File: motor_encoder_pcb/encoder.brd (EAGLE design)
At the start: 48.2 x 26.3 mm, 6 parts

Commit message: encoder pcb changes
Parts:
- moved H1 16.5 mm to (-7.62, 47.0)
- moved H2 16.5 mm to (30.5, 47.0)
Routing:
- net GND: track 0.00 -> 17.3 mm
- added copper zone on layer 1, net PLATE
- removed copper zone on layer 1, net GND
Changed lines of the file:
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@@
 </element>
 <element name="U$1" library="ee192" package="S6986" value="S6986" x="12.7" y="46.99" rot="R180"/>
-<element name="H1" library="holes" library_urn="urn:adsk.eagle:library:237" package="3,3" package3d_urn="urn:adsk.eagle:package:14278/1" value="MOUNT-HOLE3.3" x="-7.62" y="63.5"/>
-<element name="H2" library="holes" library_urn="urn:adsk.eagle:library:237" package="3,3" package3d_urn="urn:adsk.eagle:package:14278/1" value="MOUNT-HOLE3.3" x="30.48" y="63.5"/>
+<element name="H1" library="holes" library_urn="urn:adsk.eagle:library:237" package="3,3" package3d_urn="urn:adsk.eagle:package:14278/1" value="MOUNT-HOLE3.3" x="-7.62" y="46.99"/>
+<element name="H2" library="holes" library_urn="urn:adsk.eagle:library:237" package="3,3" package3d_urn="urn:adsk.eagle:package:14278/1" value="MOUNT-HOLE3.3" x="30.48" y="46.99"/>
 </elements>
 <signals>
@@
 <contactref element="U$1" pad="3"/>
 <contactref element="U$1" pad="2"/>
-<polygon width="0.0508" layer="1" isolate="0.762">
-<vertex x="-12.7" y="68.58"/>
-<vertex x="35.56" y="68.58"/>
-<vertex x="35.56" y="41.91"/>
-<vertex x="-12.7" y="41.91"/>
-</polygon>
+<wire x1="13.3" y1="46.99" x2="13.3" y2="57.75" width="0.508" layer="1"/>
+<wire x1="15.24" y1="59.69" x2="15.24" y2="63.5" width="0.508" layer="1"/>
+<wire x1="13.3" y1="57.75" x2="15.24" y2="59.69" width="0.508" layer="1"/>
+<wire x1="12.03" y1="46.99" x2="13.3" y2="46.99" width="0" layer="19" extent="1-1"/>
 </signal>
 <signal name="N$1">
@@
 <wire x1="16.51" y1="46.99" x2="16.51" y2="50.8" width="0.508" layer="1"/>
 </signal>
+<signal name="PLATE">
+<polygon width="0.0508" layer="1" isolate="0.762">
+<vertex x="-12.7" y="68.58"/>
+<vertex x="35.56" y="68.58"/>
+<vertex x="35.56" y="41.91"/>
+<vertex x="-12.7" y="41.91"/>
+</polygon>
+</signal>
 </signals>

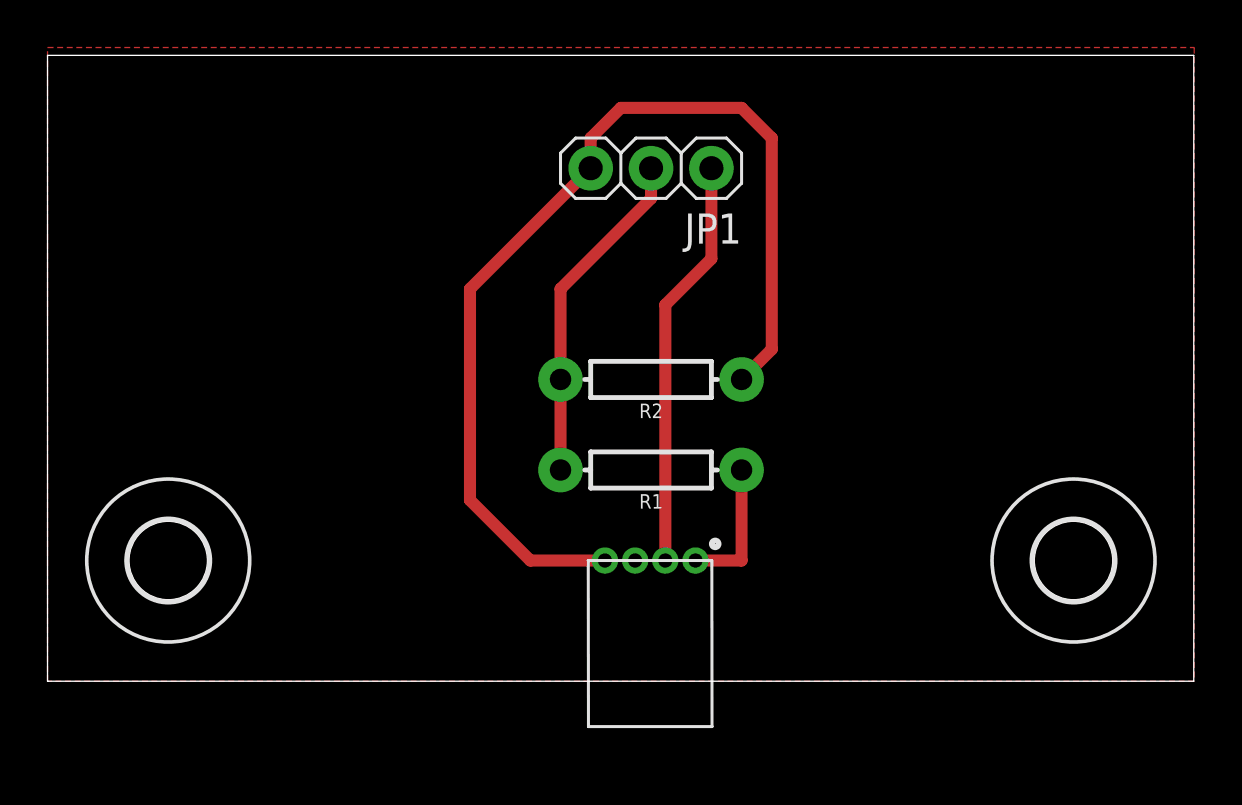
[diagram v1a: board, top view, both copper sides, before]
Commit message: new encoder PCB output
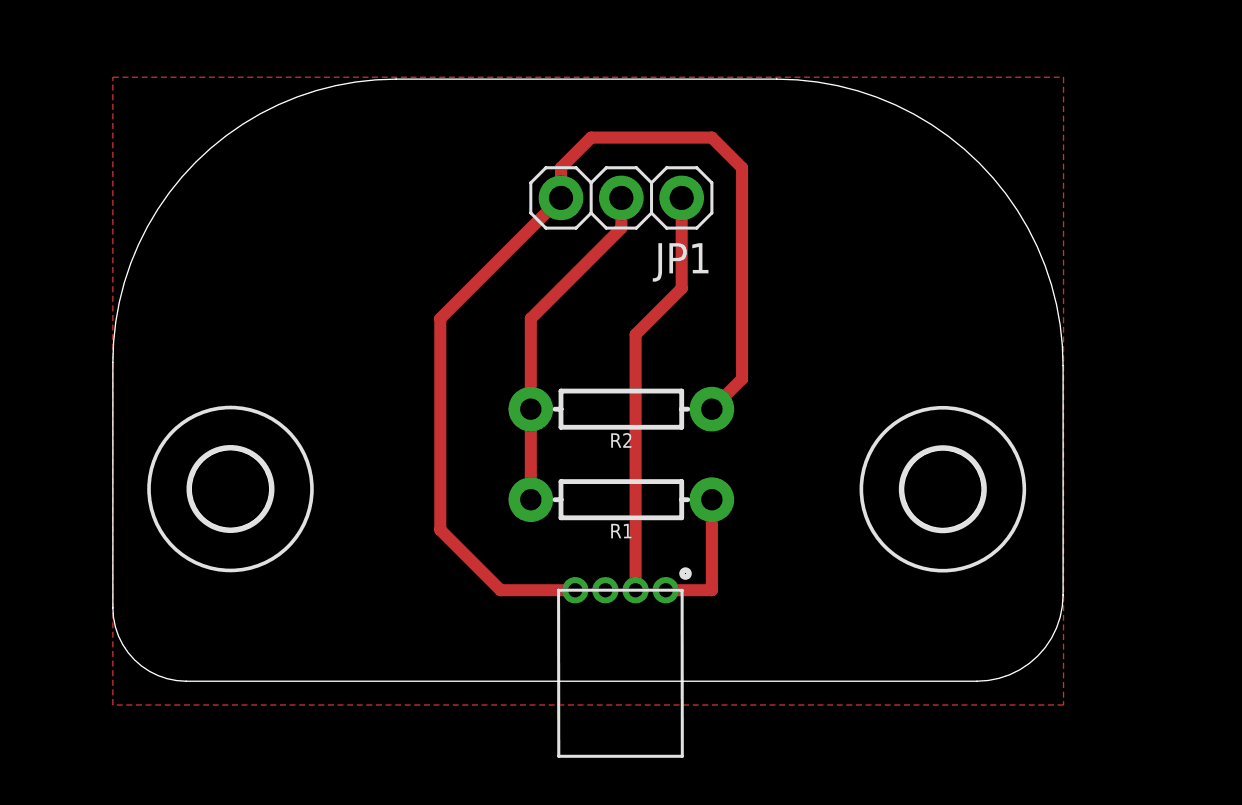
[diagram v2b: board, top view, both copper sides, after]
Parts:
- moved H2 6.26 mm to (25.0, 50.0)
- moved H1 3.99 mm to (-5.00, 50.0)
- moved JP1 1.77 mm to (11.4, 62.2)
- moved R1 1.77 mm to (11.4, 49.5)
- moved R2 1.77 mm to (11.4, 53.4)
- moved U$1 1.77 mm to (11.4, 45.7)
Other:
- board size 48.2 x 26.3 mm -> 40 x 25.3 mm
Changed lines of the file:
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@@
 <setting verticaltext="up"/>
 </settings>
-<grid distance="50" unitdist="mil" unit="mil" style="lines" multiple="2" display="yes" altdistance="5" altunitdist="mil" altunit="mil"/>
+<grid distance="5" unitdist="mm" unit="mm" style="lines" multiple="1" display="yes" altdistance="0.25" altunitdist="mm" altunit="mm"/>
 <layers>
 <layer number="1" name="Top" color="4" fill="1" visible="yes" active="yes"/>
@@
 <board>
 <plain>
-<wire x1="-12.7" y1="41.91" x2="35.54" y2="41.91" width="0" layer="20"/>
-<wire x1="35.54" y1="41.91" x2="35.54" y2="68.25" width="0" layer="20"/>
-<wire x1="35.54" y1="68.25" x2="-12.7" y2="68.25" width="0" layer="20"/>
-<wire x1="-12.7" y1="68.25" x2="-12.7" y2="41.91" width="0" layer="20"/>
+<wire x1="-9.95" y1="55.330353125" x2="-9.95" y2="45" width="0" layer="20"/>
+<wire x1="-9.95" y1="45" x2="-6.86" y2="41.91" width="0" layer="20" curve="90"/>
+<wire x1="-6.86" y1="41.91" x2="26.41303125" y2="41.91" width="0" layer="20"/>
+<wire x1="26.41303125" y1="41.91" x2="30.04" y2="45.53696875" width="0" layer="20" curve="90"/>
+<wire x1="30.04" y1="45.53696875" x2="30.04" y2="55.197646875" width="0" layer="20"/>
+<wire x1="30.04" y1="55.197646875" x2="17.987646875" y2="67.25" width="0" layer="20" curve="90"/>
+<wire x1="17.987646875" y1="67.25" x2="1.969646875" y2="67.25" width="0" layer="20"/>
+<wire x1="1.969646875" y1="67.25" x2="-9.95" y2="55.330353125" width="0" layer="20" curve="90"/>
 </plain>
 <attributes>
@@
 </class>
 </classes>
-<designrules name="default">
+<designrules name="default *">
 <description language="de">&lt;b&gt;EAGLE Design Rules&lt;/b&gt;
 &lt;p&gt;
@@
 <param name="mdViaViaSameLayer" value="6mil"/>
 <param name="mnLayersViaInSmd" value="2"/>
-<param name="mdCopperDimension" value="40mil"/>
-<param name="mdDrill" value="6mil"/>
+<param name="mdCopperDimension" value="0mil"/>
+<param name="mdDrill" value="2mil"/>
 <param name="mdSmdStop" value="0mil"/>
 <param name="msWidth" value="6mil"/>
@@
 </autorouter>
 <elements>
-<element name="JP1" library="ee192" package="1X03" value="" x="12.7" y="63.5" rot="R180">
-<attribute name="PIE-INT-REF-NUM" value="BULK-STOCK" x="12.7" y="63.5" size="1.778" layer="27" rot="R180" display="off"/>
+<element name="JP1" library="ee192" package="1X03" value="" x="11.45" y="62.25" rot="R180">
+<attribute name="PIE-INT-REF-NUM" value="BULK-STOCK" x="11.45" y="62.25" size="1.778" layer="27" rot="R180" display="off"/>
 </element>
-<element name="R1" library="SparkFun-Resistors" package="AXIAL-0.3" value="150" x="12.7" y="50.8" rot="R180">
-<attribute name="PROD_ID" value="RES-12180" x="12.7" y="50.8" size="1.778" layer="27" rot="R180" display="off"/>
+<element name="R1" library="SparkFun-Resistors" package="AXIAL-0.3" value="150" x="11.45" y="49.55" rot="R180">
+<attribute name="PROD_ID" value="RES-12180" x="11.45" y="49.55" size="1.778" layer="27" rot="R180" display="off"/>
 </element>
-<element name="R2" library="SparkFun-Resistors" package="AXIAL-0.3" value="10k" x="12.7" y="54.61" rot="R180">
-<attribute name="PROD_ID" value="RES-12180" x="12.7" y="54.61" size="1.778" layer="27" rot="R180" display="off"/>
+<element name="R2" library="SparkFun-Resistors" package="AXIAL-0.3" value="10k" x="11.45" y="53.36" rot="R180">
+<attribute name="PROD_ID" value="RES-12180" x="11.45" y="53.36" size="1.778" layer="27" rot="R180" display="off"/>
 </element>
-<element name="U$1" library="ee192" package="S6986" value="S6986" x="12.7" y="46.99" rot="R180"/>
-<element name="H1" library="holes" library_urn="urn:adsk.eagle:library:237" package="3,3" package3d_urn="urn:adsk.eagle:package:14278/1" value="MOUNT-HOLE3.3" x="-7.62" y="46.99"/>
-<element name="H2" library="holes" library_urn="urn:adsk.eagle:library:237" package="3,3" package3d_urn="urn:adsk.eagle:package:14278/1" value="MOUNT-HOLE3.3" x="30.48" y="46.99"/>
+<element name="U$1" library="ee192" package="S6986" value="S6986" x="11.45" y="45.74" rot="R180"/>
+<element name="H1" library="holes" library_urn="urn:adsk.eagle:library:237" package="3,3" package3d_urn="urn:adsk.eagle:package:14278/1" value="MOUNT-HOLE3.3" x="-5" y="50"/>
+<element name="H2" library="holes" library_urn="urn:adsk.eagle:library:237" package="3,3" package3d_urn="urn:adsk.eagle:package:14278/1" value="MOUNT-HOLE3.3" x="24.98" y="49.99"/>
 </elements>
 <signals>
@@
 <contactref element="U$1" pad="3"/>
 <contactref element="U$1" pad="2"/>
-<wire x1="13.3" y1="46.99" x2="13.3" y2="57.75" width="0.508" layer="1"/>
-<wire x1="15.24" y1="59.69" x2="15.24" y2="63.5" width="0.508" layer="1"/>
-<wire x1="13.3" y1="57.75" x2="15.24" y2="59.69" width="0.508" layer="1"/>
-<wire x1="12.03" y1="46.99" x2="13.3" y2="46.99" width="0" layer="19" extent="1-1"/>
+<wire x1="12.05" y1="45.74" x2="12.05" y2="56.5" width="0.508" layer="1"/>
+<wire x1="13.99" y1="58.44" x2="13.99" y2="62.25" width="0.508" layer="1"/>
+<wire x1="12.05" y1="56.5" x2="13.99" y2="58.44" width="0.508" layer="1"/>
+<wire x1="12.05" y1="45.74" x2="10.78" y2="45.74" width="0" layer="19" extent="1-1"/>
 </signal>
 <signal name="N$1">
@@
 <contactref element="R2" pad="P$2"/>
 <contactref element="R1" pad="P$2"/>
-<wire x1="8.89" y1="54.61" x2="8.89" y2="50.8" width="0.508" layer="1"/>
-<wire x1="8.89" y1="54.61" x2="8.89" y2="58.42" width="0.508" layer="1"/>
-<wire x1="8.89" y1="58.42" x2="12.7" y2="62.23" width="0.508" layer="1"/>
-<wire x1="12.7" y1="62.23" x2="12.7" y2="63.5" width="0.508" layer="1"/>
+<wire x1="7.64" y1="53.36" x2="7.64" y2="49.55" width="0.508" layer="1"/>
+<wire x1="7.64" y1="53.36" x2="7.64" y2="57.17" width="0.508" layer="1"/>
+<wire x1="7.64" y1="57.17" x2="11.45" y2="60.98" width="0.508" layer="1"/>
+<wire x1="11.45" y1="60.98" x2="11.45" y2="62.25" width="0.508" layer="1"/>
 </signal>
 <signal name="N$3">
@@
 <contactref element="R2" pad="P$1"/>
 <contactref element="JP1" pad="3"/>
-<wire x1="16.51" y1="54.61" x2="17.78" y2="55.88" width="0.508" layer="1"/>
-<wire x1="17.78" y1="55.88" x2="17.78" y2="64.77" width="0.508" layer="1"/>
-<wire x1="17.78" y1="64.77" x2="16.51" y2="66.04" width="0.508" layer="1"/>
-<wire x1="16.51" y1="66.04" x2="11.43" y2="66.04" width="0.508" layer="1"/>
-<wire x1="11.43" y1="66.04" x2="10.16" y2="64.77" width="0.508" layer="1"/>
-<wire x1="10.16" y1="64.77" x2="10.16" y2="63.5" width="0.508" layer="1"/>
-<wire x1="10.16" y1="63.5" x2="5.08" y2="58.42" width="0.508" layer="1"/>
-<wire x1="5.08" y1="58.42" x2="5.08" y2="49.53" width="0.508" layer="1"/>
-<wire x1="5.08" y1="49.53" x2="7.62" y2="46.99" width="0.508" layer="1"/>
-<wire x1="7.62" y1="46.99" x2="10.76" y2="46.99" width="0.508" layer="1"/>
+<wire x1="15.26" y1="53.36" x2="16.53" y2="54.63" width="0.508" layer="1"/>
+<wire x1="16.53" y1="54.63" x2="16.53" y2="63.52" width="0.508" layer="1"/>
+<wire x1="16.53" y1="63.52" x2="15.26" y2="64.79" width="0.508" layer="1"/>
+<wire x1="15.26" y1="64.79" x2="10.18" y2="64.79" width="0.508" layer="1"/>
+<wire x1="10.18" y1="64.79" x2="8.91" y2="63.52" width="0.508" layer="1"/>
+<wire x1="8.91" y1="63.52" x2="8.91" y2="62.25" width="0.508" layer="1"/>
+<wire x1="8.91" y1="62.25" x2="3.83" y2="57.17" width="0.508" layer="1"/>
+<wire x1="3.83" y1="57.17" x2="3.83" y2="48.28" width="0.508" layer="1"/>
+<wire x1="3.83" y1="48.28" x2="6.37" y2="45.74" width="0.508" layer="1"/>
+<wire x1="6.37" y1="45.74" x2="9.51" y2="45.74" width="0.508" layer="1"/>
 </signal>
 <signal name="N$6">
 <contactref element="U$1" pad="1"/>
 <contactref element="R1" pad="P$1"/>
-<wire x1="14.57" y1="46.99" x2="16.51" y2="46.99" width="0.508" layer="1"/>
-<wire x1="16.51" y1="46.99" x2="16.51" y2="50.8" width="0.508" layer="1"/>
+<wire x1="13.32" y1="45.74" x2="15.26" y2="45.74" width="0.508" layer="1"/>
+<wire x1="15.26" y1="45.74" x2="15.26" y2="49.55" width="0.508" layer="1"/>
 </signal>
 <signal name="PLATE">
 <polygon width="0.0508" layer="1" isolate="0.762">
-<vertex x="-12.7" y="68.58"/>
-<vertex x="35.56" y="68.58"/>
-<vertex x="35.56" y="41.91"/>
-<vertex x="-12.7" y="41.91"/>
+<vertex x="-9.95" y="67.33"/>
+<vertex x="30.06" y="67.33"/>
+<vertex x="30.06" y="40.91"/>
+<vertex x="-9.95" y="40.91"/>
 </polygon>
 </signal>
